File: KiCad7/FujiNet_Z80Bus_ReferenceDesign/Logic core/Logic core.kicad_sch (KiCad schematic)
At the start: 12 parts, among them IC1 7432N, IC2 7404N, IC3 7474N, IC4 7408N

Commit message: KiCad symbol library changes on logic core
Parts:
- added IC1: 74HC32N, Package_DIP:DIP-14_W7.62mm_Socket, symbol 74xx:74LS32
- IC1: value 7432N -> 74HC32N; symbol FujiNet_Z80Bus_Reference-rescue:7432N-Z80ESP-eagle-import -> 74xx:74LS32
- IC3: symbol FujiNet_Z80Bus_Reference-rescue:7474N-Z80ESP-eagle-import -> 74xx:74HC74
- IC4: value 7408N -> 74HC08N; symbol FujiNet_Z80Bus_Reference-rescue:7408N-Z80ESP-eagle-import -> 74xx:74LS08
- IC? (x2): value 7432N -> 74HC32N; symbol FujiNet_Z80Bus_Reference-rescue:7432N-Z80Decoder-eagle-import -> 74xx:74LS32
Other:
- moved on the sheet: C4, D6, IC2A, IC2D, R2

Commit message: KiCad experiment with logic core PCB
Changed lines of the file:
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@@
   (junction (at 121.285 62.23) (diameter 0) (color 0 0 0 0)
-  )
-  (junction (at 28.448 147.828) (diameter 0) (color 0 0 0 0)
-  )
-  (junction (at 28.448 122.428) (diameter 0) (color 0 0 0 0)
   )
   (junction (at 120.65 118.872) (diameter 0) (color 0 0 0 0)
@@
     (stroke (width 0) (type default))
   )
-  (wire (pts (xy 28.448 122.428) (xy 19.05 122.428))
-    (stroke (width 0) (type default))
-  )
   (wire (pts (xy 217.17 83.82) (xy 223.52 83.82))
     (stroke (width 0) (type default))
@@
     (stroke (width 0) (type default))
   )
-  (wire (pts (xy 39.37 147.828) (xy 28.448 147.828))
-    (stroke (width 0) (type default))
-  )
   (wire (pts (xy 15.748 97.917) (xy 46.228 97.917))
     (stroke (width 0) (type default))
@@
     (stroke (width 0) (type default))
   )
-  (wire (pts (xy 28.448 147.828) (xy 19.558 147.828))
+  (wire (pts (xy 19.558 147.828) (xy 39.37 147.828))
     (stroke (width 0) (type default))
   )
@@
     (stroke (width 0) (type default))
   )
-  (wire (pts (xy 39.37 122.428) (xy 28.448 122.428))
+  (wire (pts (xy 19.05 122.428) (xy 39.37 122.428))
     (stroke (width 0) (type default))
   )
@@
       (project "Logic core"
         (path "/648e0b91-567a-4972-a379-57b42123c6d5"
-          (reference "IC1") (unit 1)
+          (reference "IC1") (unit 7)
         )
       )
@@
       (project "Logic core"
         (path "/648e0b91-567a-4972-a379-57b42123c6d5"
-          (reference "#PWR01") (unit 1)
+          (reference "#PWR03") (unit 1)
         )
       )
@@
       (project "Logic core"
         (path "/648e0b91-567a-4972-a379-57b42123c6d5"
-          (reference "IC5") (unit 1)
+          (reference "IC6") (unit 1)
         )
       )
@@
       (project "Logic core"
         (path "/648e0b91-567a-4972-a379-57b42123c6d5"
-          (reference "IC2") (unit 4)
+          (reference "IC3") (unit 4)
         )
       )
@@
       (project "Logic core"
         (path "/648e0b91-567a-4972-a379-57b42123c6d5"
-          (reference "IC3") (unit 2)
+          (reference "IC4") (unit 2)
         )
       )
@@
       (project "Logic core"
         (path "/648e0b91-567a-4972-a379-57b42123c6d5"
-          (reference "IC4") (unit 1)
+          (reference "IC2") (unit 5)
         )
       )
@@
       (project "Logic core"
         (path "/648e0b91-567a-4972-a379-57b42123c6d5"
-          (reference "#PWR04") (unit 1)
+          (reference "#PWR06") (unit 1)
         )
       )
@@
       (project "Logic core"
         (path "/648e0b91-567a-4972-a379-57b42123c6d5"
-          (reference "#PWR03") (unit 1)
+          (reference "#PWR02") (unit 1)
         )
       )
@@
       (project "Logic core"
         (path "/648e0b91-567a-4972-a379-57b42123c6d5"
-          (reference "IC3") (unit 1)
+          (reference "IC4") (unit 1)
         )
       )
@@
       (project "Logic core"
         (path "/648e0b91-567a-4972-a379-57b42123c6d5"
-          (reference "#PWR03") (unit 1)
+          (reference "#PWR04") (unit 1)
         )
       )
@@
       (project "Logic core"
         (path "/648e0b91-567a-4972-a379-57b42123c6d5"
-          (reference "IC4") (unit 1)
+          (reference "IC5") (unit 1)
         )
       )
@@
       (project "Logic core"
         (path "/648e0b91-567a-4972-a379-57b42123c6d5"
-          (reference "#PWR02") (unit 1)
+          (reference "#PWR05") (unit 1)
         )
       )
@@
       (project "Logic core"
         (path "/648e0b91-567a-4972-a379-57b42123c6d5"
-          (reference "IC2") (unit 3)
-        )
-      )
+          (reference "IC3") (unit 3)
+        )
+      )

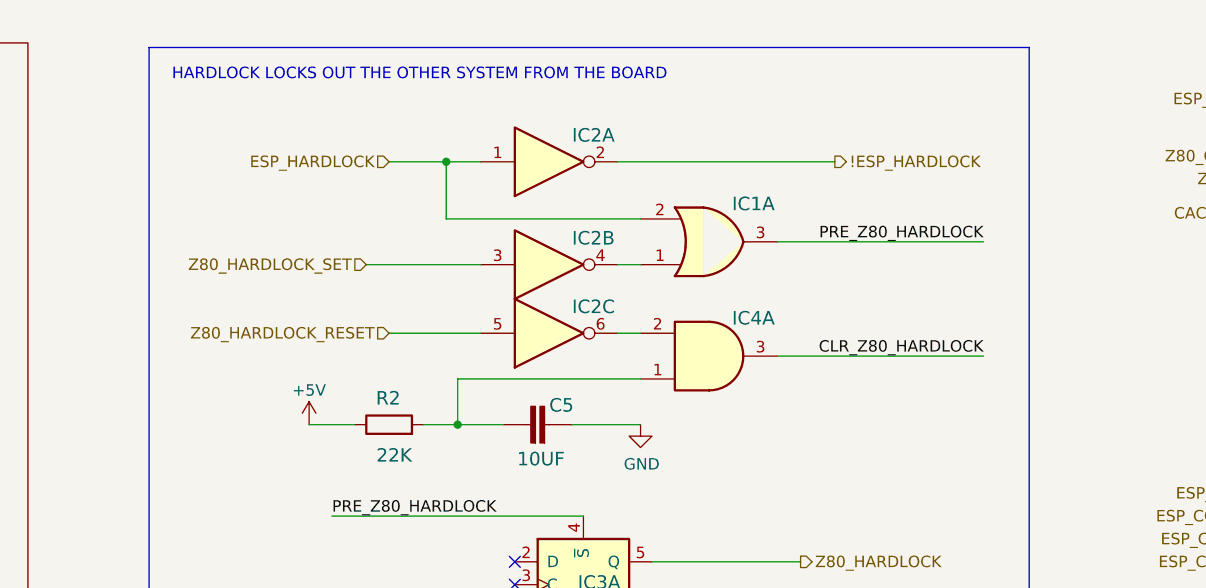
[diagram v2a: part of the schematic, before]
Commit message: KiCad diode OR gate example added to Core
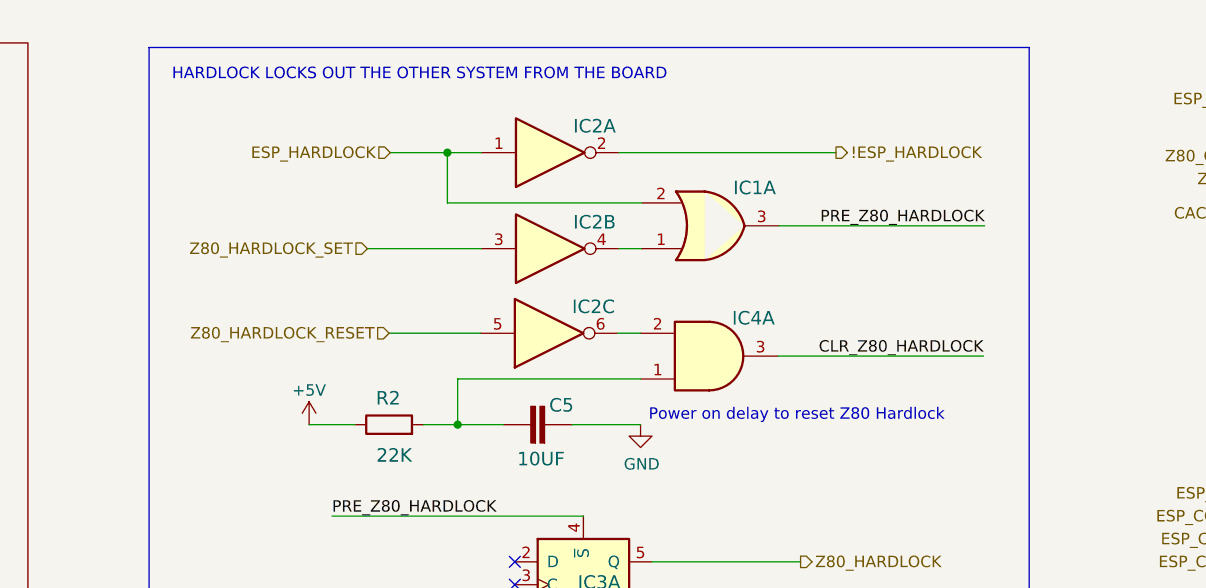
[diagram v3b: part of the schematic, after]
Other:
- note added: "Power on delay to reset Z80 Hardlock"
- moved on the sheet: IC1A, IC2A, IC2B
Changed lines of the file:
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@@
   (junction (at 120.65 124.206) (diameter 0) (color 0 0 0 0)
   )
+  (junction (at 120.142 32.004) (diameter 0) (color 0 0 0 0)
+  )
   (junction (at 121.285 62.23) (diameter 0) (color 0 0 0 0)
   )
   (junction (at 120.65 118.872) (diameter 0) (color 0 0 0 0)
-  )
-  (junction (at 120.015 33.02) (diameter 0) (color 0 0 0 0)
   )
   (no_connect (at 127.635 80.01))
@@
   (no_connect (at 127.254 111.506))
   (no_connect (at 127.254 114.046))
-  (wire (pts (xy 139.065 44.45) (xy 141.605 44.45))
+  (wire (pts (xy 139.192 42.672) (xy 141.732 42.672))
     (stroke (width 0) (type default))
   )
@@
     (stroke (width 0) (type default))
   )
-  (wire (pts (xy 139.065 33.02) (xy 163.195 33.02))
+  (wire (pts (xy 139.192 32.004) (xy 163.322 32.004))
     (stroke (width 0) (type default))
   )
@@
     (stroke (width 0) (type default))
   )
-  (wire (pts (xy 141.605 39.37) (xy 120.015 39.37))
+  (wire (pts (xy 141.732 37.592) (xy 120.142 37.592))
     (stroke (width 0) (type default))
   )
@@
     (stroke (width 0) (type default))
   )
-  (wire (pts (xy 123.825 44.45) (xy 111.125 44.45))
+  (wire (pts (xy 123.952 42.672) (xy 111.252 42.672))
     (stroke (width 0) (type default))
   )
@@
     (stroke (width 0) (type default))
   )
-  (wire (pts (xy 156.845 41.91) (xy 179.705 41.91))
+  (wire (pts (xy 156.972 40.132) (xy 179.832 40.132))
     (stroke (width 0) (type default))
   )
@@
     (stroke (width 0) (type default))
   )
-  (wire (pts (xy 120.015 33.02) (xy 113.665 33.02))
+  (wire (pts (xy 120.142 32.004) (xy 113.792 32.004))
     (stroke (width 0) (type default))
   )
@@
     (stroke (width 0) (type default))
   )
-  (wire (pts (xy 120.015 39.37) (xy 120.015 33.02))
+  (wire (pts (xy 120.142 37.592) (xy 120.142 32.004))
     (stroke (width 0) (type default))
   )
@@
     (stroke (width 0) (type default))
   )
-  (wire (pts (xy 123.825 33.02) (xy 120.015 33.02))
+  (wire (pts (xy 123.952 32.004) (xy 120.142 32.004))
     (stroke (width 0) (type default))
   )
@@
     (effects (font (size 1.27 1.27)) (justify left bottom))
   )
+  (text "Power on delay to reset Z80 Hardlock\n" (at 142.494 61.976 0)
+    (effects (font (size 1.27 1.27)) (justify left bottom))
+  )
   (text "HOLD THE Z80 WITH A WAIT" (at 89.535 100.965 0)
     (effects (font (size 1.27 1.27)) (justify left bottom))
@@
     (effects (font (size 1.27 1.27)) (justify left bottom))
   )
-  (label "PRE_Z80_HARDLOCK" (at 179.705 41.91 180) (fields_autoplaced)
+  (label "PRE_Z80_HARDLOCK" (at 179.832 40.132 180) (fields_autoplaced)
     (effects (font (size 1.27 1.27)) (justify right bottom))
   )
@@
     (effects (font (size 1.27 1.27)) (justify right))
   )
-  (hierarchical_label "ESP_HARDLOCK" (shape input) (at 113.665 33.02 180) (fields_autoplaced)
+  (hierarchical_label "ESP_HARDLOCK" (shape input) (at 113.792 32.004 180) (fields_autoplaced)
     (effects (font (size 1.27 1.27)) (justify right))
   )
@@
     (effects (font (size 1.27 1.27)) (justify right))
   )
-  (hierarchical_label "!ESP_HARDLOCK" (shape output) (at 163.195 33.02 0) (fields_autoplaced)
+  (hierarchical_label "!ESP_HARDLOCK" (shape output) (at 163.322 32.004 0) (fields_autoplaced)
     (effects (font (size 1.27 1.27)) (justify left))
   )
@@
     (effects (font (size 1.27 1.27)) (justify right))
   )
-  (hierarchical_label "Z80_HARDLOCK_SET" (shape input) (at 111.125 44.45 180) (fields_autoplaced)
+  (hierarchical_label "Z80_HARDLOCK_SET" (shape input) (at 111.252 42.672 180) (fields_autoplaced)
     (effects (font (size 1.27 1.27)) (justify right))
   )
@@
     (effects (font (size 1.27 1.27)) (justify left))
   )
-  (symbol (lib_id "74xx:74HC04") (at 131.445 44.45 0) (mirror x) (unit 2)
-    (in_bom yes) (on_board yes) (dnp no)
-    (property "Reference" "IC2" (at 133.985 40.64 0)
+  (symbol (lib_id "74xx:74HC04") (at 131.572 42.672 0) (mirror x) (unit 2)
+    (in_bom yes) (on_board yes) (dnp no)
+    (property "Reference" "IC2" (at 134.112 38.862 0)
       (effects (font (size 1.4986 1.4986)) (justify left bottom))
     )
-    (property "Value" "7404N" (at 133.985 39.37 0)
+    (property "Value" "7404N" (at 134.112 37.592 0)
       (effects (font (size 1.4986 1.4986)) (justify left bottom) hide)
     )
-    (property "Footprint" "Package_DIP:DIP-14_W7.62mm_Socket" (at 131.445 44.45 0)
-      (effects (font (size 1.27 1.27)) hide)
-    )
-    (property "Datasheet" "https://assets.nexperia.com/documents/data-sheet/74HC_HCT04.pdf" (at 131.445 44.45 0)
+    (property "Footprint" "Package_DIP:DIP-14_W7.62mm_Socket" (at 131.572 42.672 0)
+      (effects (font (size 1.27 1.27)) hide)
+    )
+    (property "Datasheet" "https://assets.nexperia.com/documents/data-sheet/74HC_HCT04.pdf" (at 131.572 42.672 0)
       (effects (font (size 1.27 1.27)) hide)
     )
@@
     )
   )
-  (symbol (lib_id "74xx:74HC04") (at 131.445 33.02 0) (mirror x) (unit 1)
-    (in_bom yes) (on_board yes) (dnp no)
-    (property "Reference" "IC2" (at 133.985 29.21 0)
+  (symbol (lib_id "74xx:74HC04") (at 131.572 32.004 0) (mirror x) (unit 1)
+    (in_bom yes) (on_board yes) (dnp no)
+    (property "Reference" "IC2" (at 134.112 28.194 0)
       (effects (font (size 1.4986 1.4986)) (justify left bottom))
     )
-    (property "Value" "7404N" (at 133.985 27.94 0)
+    (property "Value" "7404N" (at 134.112 26.924 0)
       (effects (font (size 1.4986 1.4986)) (justify left bottom) hide)
     )
-    (property "Footprint" "Package_DIP:DIP-14_W7.62mm_Socket" (at 131.445 33.02 0)
-      (effects (font (size 1.27 1.27)) hide)
-    )
-    (property "Datasheet" "https://assets.nexperia.com/documents/data-sheet/74HC_HCT04.pdf" (at 131.445 33.02 0)
+    (property "Footprint" "Package_DIP:DIP-14_W7.62mm_Socket" (at 131.572 32.004 0)
+      (effects (font (size 1.27 1.27)) hide)
+    )
+    (property "Datasheet" "https://assets.nexperia.com/documents/data-sheet/74HC_HCT04.pdf" (at 131.572 32.004 0)
       (effects (font (size 1.27 1.27)) hide)
     )
@@
     )
   )
-  (symbol (lib_id "74xx:74LS32") (at 149.225 41.91 0) (mirror x) (unit 1)
-    (in_bom yes) (on_board yes) (dnp no)
-    (property "Reference" "IC1" (at 151.765 36.83 0)
+  (symbol (lib_id "74xx:74LS32") (at 149.352 40.132 0) (mirror x) (unit 1)
+    (in_bom yes) (on_board yes) (dnp no)
+    (property "Reference" "IC1" (at 151.892 35.052 0)
       (effects (font (size 1.4986 1.4986)) (justify left bottom))
     )
-    (property "Value" "74HC32N" (at 151.765 36.83 0)
+    (property "Value" "74HC32N" (at 151.892 35.052 0)
       (effects (font (size 1.4986 1.4986)) (justify left bottom) hide)
     )
-    (property "Footprint" "Package_DIP:DIP-14_W7.62mm_Socket" (at 149.225 41.91 0)
-      (effects (font (size 1.27 1.27)) hide)
-    )
-    (property "Datasheet" "http://www.ti.com/lit/gpn/sn74LS32" (at 149.225 41.91 0)
-      (effects (font (size 1.27 1.27)) hide)
-    )
+    (property "Footprint" "Package_DIP:DIP-14_W7.62mm_Socket" (at 149.352 40.132 0)
+      (effects (font (size 1.27 1.27)) hide)
+    )
+    (property "Datasheet" "http://www.ti.com/lit/gpn/sn74LS32" (at 149.352 40.132 0)
+      (effects (font (size 1.27 1.27)) hide)
+    )

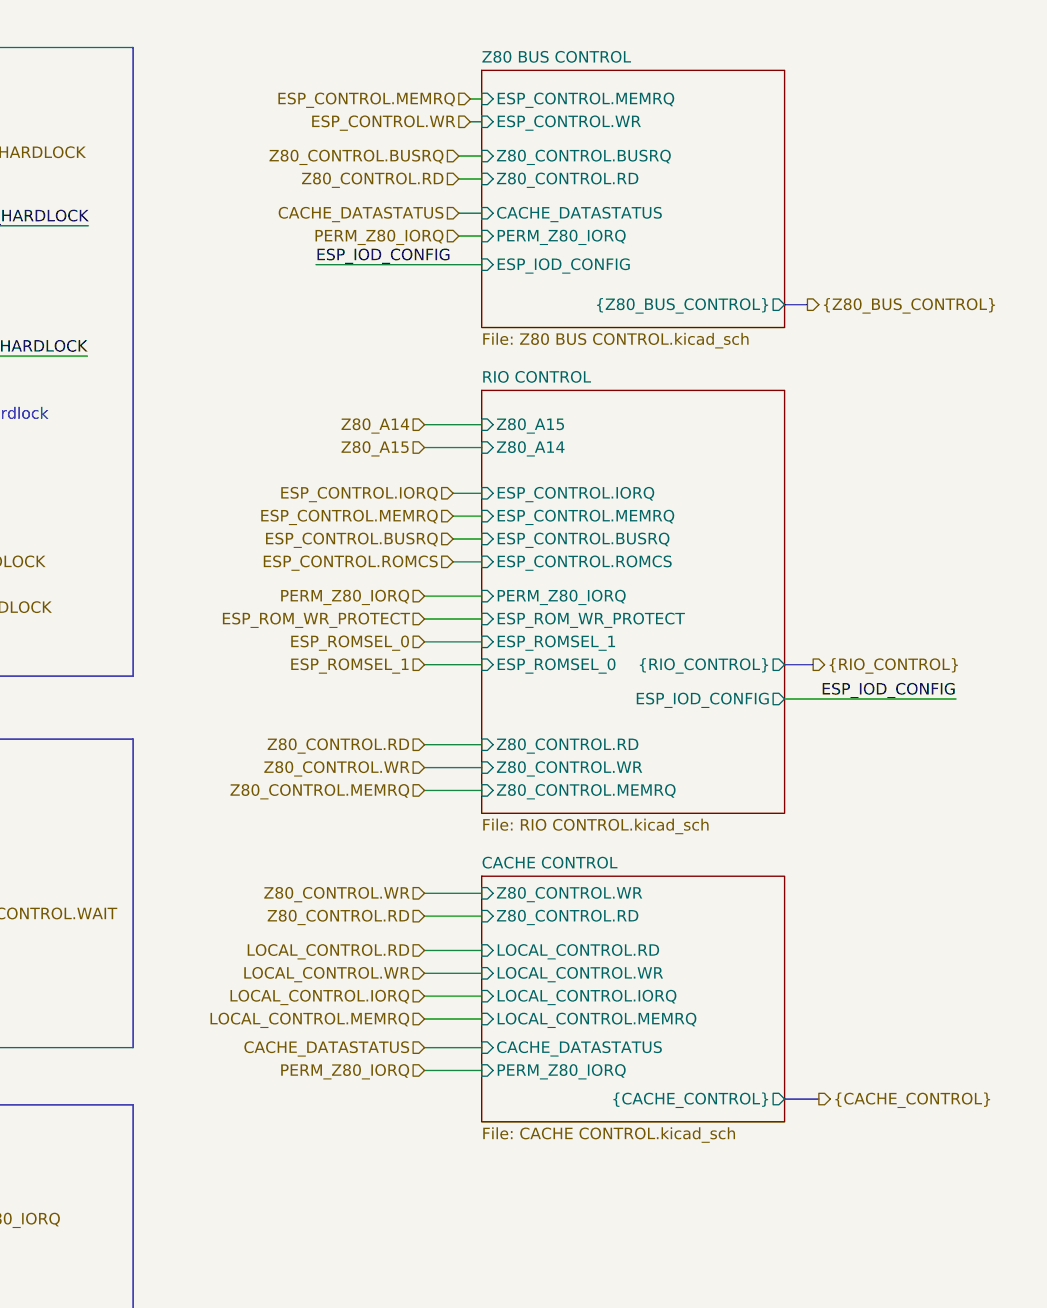
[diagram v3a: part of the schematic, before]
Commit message: KiCad repairing grid alignment
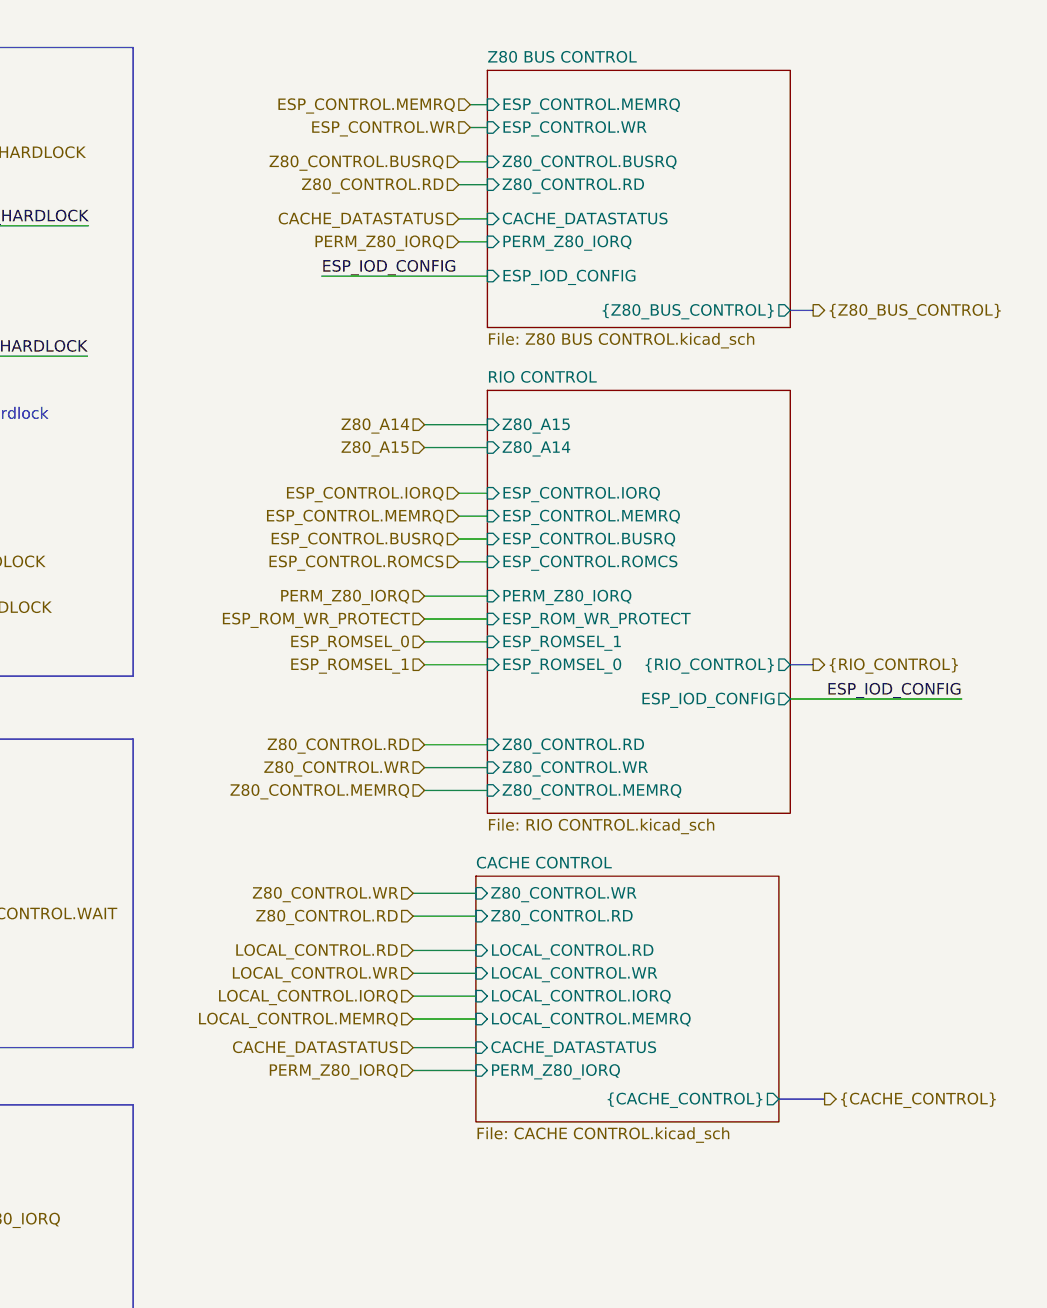
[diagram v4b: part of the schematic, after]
